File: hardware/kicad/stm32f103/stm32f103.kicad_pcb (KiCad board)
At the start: 2 copper layers, 67.3 x 69.2 mm, 114 parts, among them IC1 AT24CS02-SSHM, K1 RELAY_1RT, K2 RELAY_1RT, P1 5VIN, P10 SWD, P2 LOOP1, P3 LOOP2, P4 RELAY OUT 1, P5 TTL OUT 1, P6 RELAY OUT 2, P7 TTL OUT 2, P8 UART, P9 I2C, Q1 BSS138, Q2 BC817-40, Q3 BSS138, Q4 BC817-40, Q5 BC817-40, Q6 BC817-40, Q7 BC817-40, Q8 BC817-40, SW1 TACTILE_SW, SW2 TACTILE_SW, SW3 RESET, T1 78601/9C, T2 78601/9C, U1 LM1117-3.3, U2 STM32F030F4Px, U3 MCP23017, Y1 12MHz

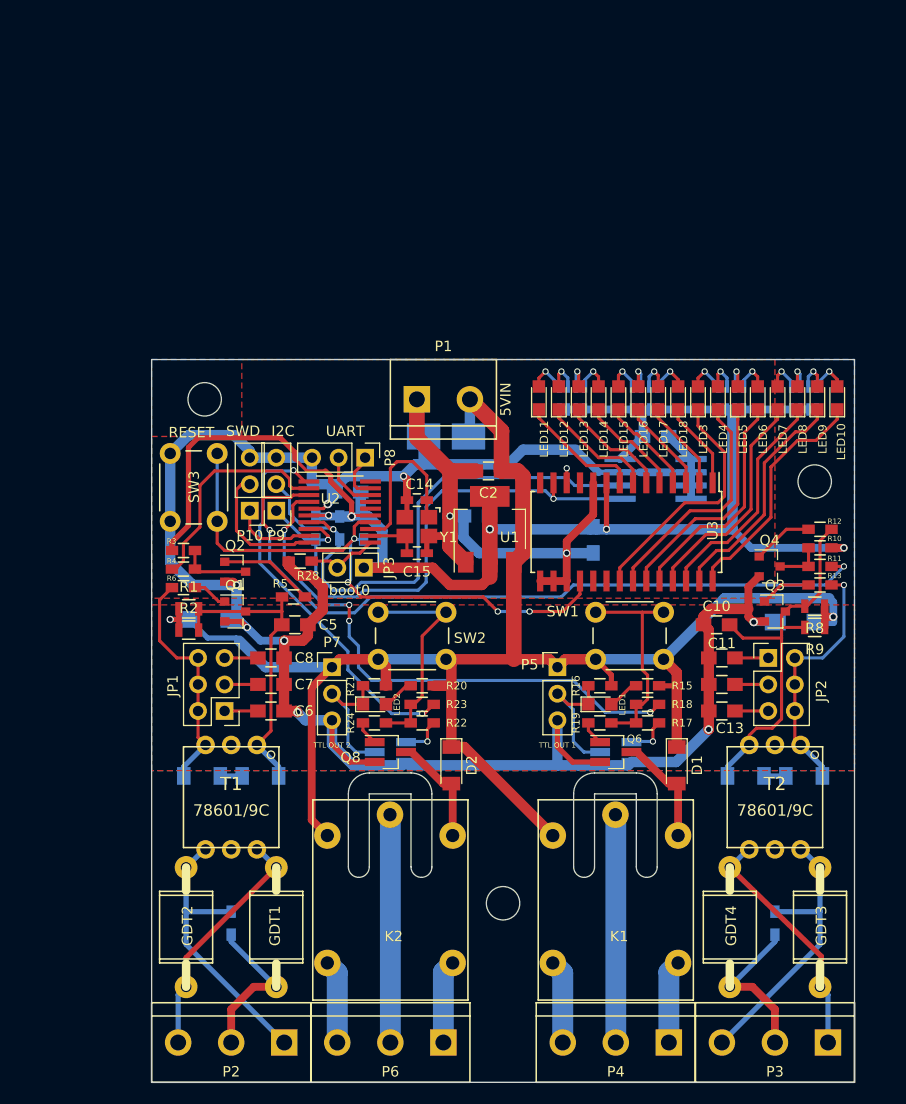
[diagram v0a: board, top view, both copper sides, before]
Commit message: hardware/kicad/stm32f103: MCU/LED block ready
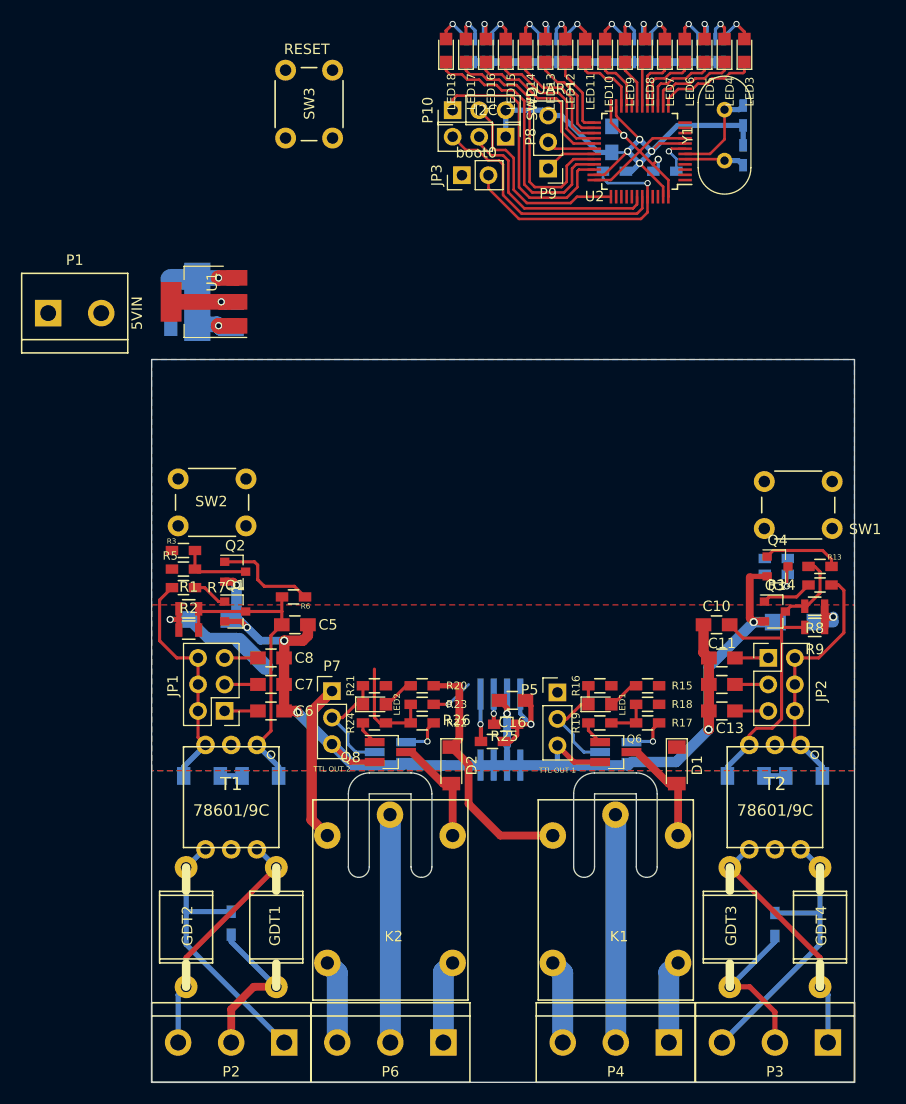
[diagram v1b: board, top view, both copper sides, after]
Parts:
- removed C18: 100n, Capacitors_SMD:C_0805_HandSoldering
- removed REF** (x3): MountingHole_3.2mm_M3, Mounting_Holes:MountingHole_3.2mm_M3
- removed U3: MCP23017, Housings_SOIC:SOIC-28W_7.5x17.9mm_Pitch1.27mm
- C14, C15, C2, R10, R12, R28: moved to B.Cu
- C16, R26: moved to F.Cu
- P8: value UART -> I2C
- P9: value I2C -> UART
- R11, R4: value 4.7k -> 1.8M; moved to B.Cu
- R13, R6: value 1k -> 4.7k
- R14, R7: value 1.8M -> 1k; moved to F.Cu
- R25: value 10k -> 4.7k; moved to F.Cu
- R27: value 4.7k -> 10k
- U2: value STM32F030F4Px -> STM32F103C8Tx; footprint Housings_SSOP:TSSOP-20_4.4x6.5mm_Pitch0.65mm_Handsoldering -> Housings_QFP:LQFP-48_7x7mm_Pitch0.5mm
- Y1: value 12MHz -> Crystal_Small; footprint Crystals:Crystal_SMD_3225_4Pads -> Crystals:Crystal_HC49-U_Vertical
- moved C15 52.3 mm to (92.2, 69.3), turned to 270 degrees
- moved R28 48.0 mm to (79.9, 74.7), turned to 0 degrees
- moved R27 47.8 mm to (84.7, 74.7), turned to 0 degrees
- moved Y1 45.8 mm to (90.4, 73.7), turned to 90 degrees
- moved C14 45.5 mm to (92.2, 73.2), turned to 90 degrees
- moved U2 44.9 mm to (82.3, 72.8)
- moved P10 43.0 mm to (64.4, 68.8), turned to 90 degrees
- moved P9 41.9 mm to (73.5, 74.4)
- moved LED18 40.0 mm to (63.8, 63.1)
- moved LED10 40.0 mm to (79.0, 63.1)
- moved JP3 38.7 mm to (65.3, 75.1), turned to 90 degrees
- moved C17 38.4 mm to (79.6, 71.6)
- moved SW3 38.3 mm to (48.4, 71.5)
- moved LED17 38.0 mm to (65.7, 63.1)
- moved LED9 38.0 mm to (80.9, 63.1)
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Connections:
- GDT4 pad 1: Net-(GDT3-Pad2) -> Net-(GDT4-Pad1)
- GDT4 pad 2: Net-(GDT4-Pad2) -> Net-(GDT3-Pad1)
- LED10 pad 1: Net-(LED10-Pad1) -> /MCU/LD18
- LED11 pad 1: Net-(LED11-Pad1) -> /MCU/LD21
- LED12 pad 1: Net-(LED12-Pad1) -> /MCU/LD22
- LED13 pad 1: Net-(LED13-Pad1) -> /MCU/LD23
- LED14 pad 1: Net-(LED14-Pad1) -> /MCU/LD24
- LED15 pad 1: Net-(LED15-Pad1) -> /MCU/LD25
- LED16 pad 1: Net-(LED16-Pad1) -> /MCU/LD26
- LED17 pad 1: Net-(LED17-Pad1) -> /MCU/LD27
- LED18 pad 1: Net-(LED18-Pad1) -> /MCU/LD28
- LED3 pad 1: Net-(LED3-Pad1) -> /MCU/LD11
- LED4 pad 1: Net-(LED4-Pad1) -> /MCU/LD12
- LED5 pad 1: Net-(LED5-Pad1) -> /MCU/LD13
- LED6 pad 1: Net-(LED6-Pad1) -> /MCU/LD14
- LED7 pad 1: Net-(LED7-Pad1) -> /MCU/LD15
- LED8 pad 1: Net-(LED8-Pad1) -> /MCU/LD16
- LED9 pad 1: Net-(LED9-Pad1) -> /MCU/LD17
- P3 pad 1: Net-(GDT3-Pad2) -> Net-(GDT3-Pad1)
- P3 pad 2: Net-(GDT4-Pad2) -> Net-(GDT3-Pad2)
- P3 pad 3: Net-(GDT3-Pad1) -> Net-(GDT4-Pad1)
- P8 pad 1: /MCU/RXD -> GND
- P8 pad 2: /MCU/TXD -> /EEPROM/scl
- P8 pad 3: GND -> /EEPROM/sda
- P9 pad 1: /EEPROM/sda -> /MCU/RXD
- P9 pad 2: /EEPROM/scl -> /MCU/TXD
- R11 pad 1: /colpitts/osc1 -> Net-(GDT4-Pad1)
- R11 pad 2: Net-(Q4-Pad3) -> Net-(GDT3-Pad2)
- R12 pad 1: Net-(C10-Pad1) -> /colpitts/osc1
- R12 pad 2: Net-(Q4-Pad1) -> Net-(Q4-Pad3)
- R13 pad 1: Net-(Q3-Pad1) -> Net-(C10-Pad1)
- R13 pad 2: Net-(JP2-Pad2) -> Net-(Q4-Pad1)
- R14 pad 1: Net-(GDT3-Pad1) -> Net-(Q3-Pad1)
- R14 pad 2: Net-(GDT4-Pad2) -> Net-(JP2-Pad2)
- R25 pad 2: /MCU/reset -> /EEPROM/scl
- R26 pad 2: /EEPROM/scl -> /EEPROM/sda
- R27 pad 2: /EEPROM/sda -> Net-(R27-Pad2)
- R4 pad 1: /MCU/osc1 -> Net-(GDT2-Pad1)
- R4 pad 2: Net-(Q2-Pad3) -> Net-(GDT1-Pad2)
- R5 pad 1: Net-(C5-Pad1) -> /MCU/osc1
- R5 pad 2: Net-(Q2-Pad1) -> Net-(Q2-Pad3)
- R6 pad 1: Net-(Q1-Pad1) -> Net-(C5-Pad1)
- R6 pad 2: Net-(JP1-Pad2) -> Net-(Q2-Pad1)
- R7 pad 1: Net-(GDT2-Pad1) -> Net-(Q1-Pad1)
- R7 pad 2: Net-(GDT1-Pad2) -> Net-(JP1-Pad2)
- RN1 pad 1: Net-(LED3-Pad2) -> Net-(LED6-Pad2)
- RN1 pad 2: Net-(LED4-Pad2) -> Net-(LED5-Pad2)
- RN1 pad 3: Net-(LED5-Pad2) -> Net-(LED4-Pad2)
- RN1 pad 4: Net-(LED6-Pad2) -> Net-(LED3-Pad2)
- RN2 pad 1: Net-(LED7-Pad2) -> Net-(LED10-Pad2)
- RN2 pad 2: Net-(LED8-Pad2) -> Net-(LED9-Pad2)
- RN2 pad 3: Net-(LED9-Pad2) -> Net-(LED8-Pad2)
- RN2 pad 4: Net-(LED10-Pad2) -> Net-(LED7-Pad2)
- RN3 pad 1: Net-(LED11-Pad2) -> Net-(LED14-Pad2)
- RN3 pad 2: Net-(LED12-Pad2) -> Net-(LED13-Pad2)
- RN3 pad 3: Net-(LED13-Pad2) -> Net-(LED12-Pad2)
- RN3 pad 4: Net-(LED14-Pad2) -> Net-(LED11-Pad2)
- RN4 pad 1: Net-(LED15-Pad2) -> Net-(LED18-Pad2)
- RN4 pad 2: Net-(LED16-Pad2) -> Net-(LED17-Pad2)
- RN4 pad 3: Net-(LED17-Pad2) -> Net-(LED16-Pad2)
- RN4 pad 4: Net-(LED18-Pad2) -> Net-(LED15-Pad2)
- SW3 pad 2: /MCU/reset -> Net-(R27-Pad2)
- T2 pad 4: Net-(GDT3-Pad2) -> Net-(GDT3-Pad1)
- T2 pad 6: Net-(GDT3-Pad1) -> Net-(GDT4-Pad1)
- U2 pad 1: Net-(JP3-Pad2) -> (no net)
- U2 pad 10: (no net) -> /MCU/osc1
- U2 pad 11: /MCU/active1 -> (no net)
- U2 pad 12: /MCU/osc1 -> /colpitts/osc1
- U2 pad 13: /colpitts/osc1 -> /MCU/LD11
- U2 pad 14: /outputs/active1 -> /MCU/LD12
- U2 pad 15: GND -> /MCU/LD13
- U2 pad 16: +3V3 -> /MCU/LD14
- U2 pad 17: /EEPROM/scl -> /MCU/LD15
- U2 pad 18: /EEPROM/sda -> /MCU/LD16
- U2 pad 19: /MCU/SWD -> /MCU/LD17
- U2 pad 2: Net-(C15-Pad1) -> (no net)
- U2 pad 20: /MCU/SWC -> (no net)
- U2 pad 3: Net-(C14-Pad1) -> /MCU/active1
- U2 pad 4: /MCU/reset -> /outputs/active1
- U2 pad 5: +3V3 -> Net-(C14-Pad1)
- U2 pad 6: (no net) -> Net-(C15-Pad1)
- U2 pad 7: (no net) -> Net-(R27-Pad2)
- U2 pad 8: /MCU/TXD -> GND
- U2 pad 9: /MCU/RXD -> +3V3
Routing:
- net +5V: track 169.3 -> 67.3 mm, vias 2 -> 3
- net GND: track 272.5 -> 177.1 mm, vias 10 -> 12
- net +3V3: track 155.9 -> 67.1 mm, vias 5 -> 4
- net /colpitts/osc1: track 70.8 -> 0.00 mm, vias 2 -> 0
- net /MCU/reset: track 56.1 -> 0.00 mm, vias 4 -> 0
- net /outputs/active1: track 52.8 -> 0.00 mm, vias 4 -> 0
- net /MCU/active1: track 37.6 -> 4.13 mm, vias 2 -> 1
- net /EEPROM/scl: track 56.8 -> 23.9 mm, vias 2 -> 1
- net Net-(GDT4-Pad1): track 0.00 -> 27.6 mm
- net /MCU/LD28: track 0.00 -> 26.5 mm
- net /EEPROM/sda: track 53.4 -> 28.8 mm, vias 2 -> 1
- net /MCU/LD27: track 0.00 -> 24.4 mm
- net Net-(LED3-Pad1): track 23.5 -> 0.00 mm
- net Net-(LED10-Pad1): track 22.9 -> 0.00 mm
- net Net-(LED4-Pad1): track 22.6 -> 0.00 mm
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- removed copper zone on F.Cu, net +3V3
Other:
- net class Default: clearance 0.25 -> 0.17; trace_width 0.3 -> 0.25
- net class Power: clearance 0.25 -> 0.24
- rule trace_clearance: 0.25 -> 0.17

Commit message: hardware/kicad/stm32f103: Almost there...
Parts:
- added REF**: MountingHole_3.2mm_M3, Mounting_Holes:MountingHole_3.2mm_M3, F.Cu at (98.8, 101.6)
- added REF**: MountingHole_3.2mm_M3, Mounting_Holes:MountingHole_3.2mm_M3, F.Cu at (39.6, 101.6)
- added REF**: MountingHole_3.2mm_M3, Mounting_Holes:MountingHole_3.2mm_M3, F.Cu at (69.2, 144.7)
- C16: moved to B.Cu
- C17: moved to F.Cu
- moved SW3 55.7 mm to (89.4, 109.2)
- moved C17 48.9 mm to (70.1, 119.6), turned to 180 degrees
- moved R28 40.9 mm to (64.3, 112.5), turned to 90 degrees
- moved JP3 38.0 mm to (59.7, 112.6)
- moved LED17 38.0 mm to (60.1, 100.7)
- moved LED4 38.0 mm to (84.8, 100.7)
- moved LED5 38.0 mm to (82.9, 100.7)
- moved LED6 38.0 mm to (81.0, 100.7)
- moved LED7 38.0 mm to (79.1, 100.7)
- moved LED8 38.0 mm to (77.2, 100.7)
- moved P9 38.0 mm to (67.9, 112.0)
- moved R27 38.0 mm to (79.1, 112.3)
- moved RN3 38.0 mm to (68.3, 100.7)
- moved U2 38.0 mm to (76.7, 110.4)
- moved Y1 38.0 mm to (84.8, 111.3)
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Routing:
- net +5V: track 67.3 -> 183.3 mm
- net +3V3: track 67.1 -> 145.9 mm, vias 4 -> 5
- net /MCU/osc1: track 0.00 -> 55.1 mm, vias 0 -> 2
- net GND: track 177.1 -> 224.1 mm
- net /MCU/active1: track 4.13 -> 33.9 mm, vias 1 -> 2
- net Net-(R27-Pad2): track 3.86 -> 27.3 mm
- net /outputs/active1: track 0.00 -> 18.7 mm, vias 0 -> 2
- net /colpitts/osc1: track 0.00 -> 17.7 mm, vias 0 -> 1
- net Net-(R17-Pad2): track 4.15 -> 15.6 mm
- net Net-(R22-Pad2): track 10.1 -> 16.5 mm
- net Net-(JP3-Pad2): track 25.9 -> 22.3 mm, vias 1 -> 0
- net /EEPROM/scl: track 23.9 -> 27.5 mm, vias 1 -> 2
- net /EEPROM/sda: track 28.8 -> 31.8 mm, vias 1 -> 2
- net Net-(LED2-Pad1): track 11.3 -> 9.71 mm
- added copper zone on F.Cu, net +3V3
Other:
- board size 67.3 x 69.2 mm -> 67.3 x 64.4 mm

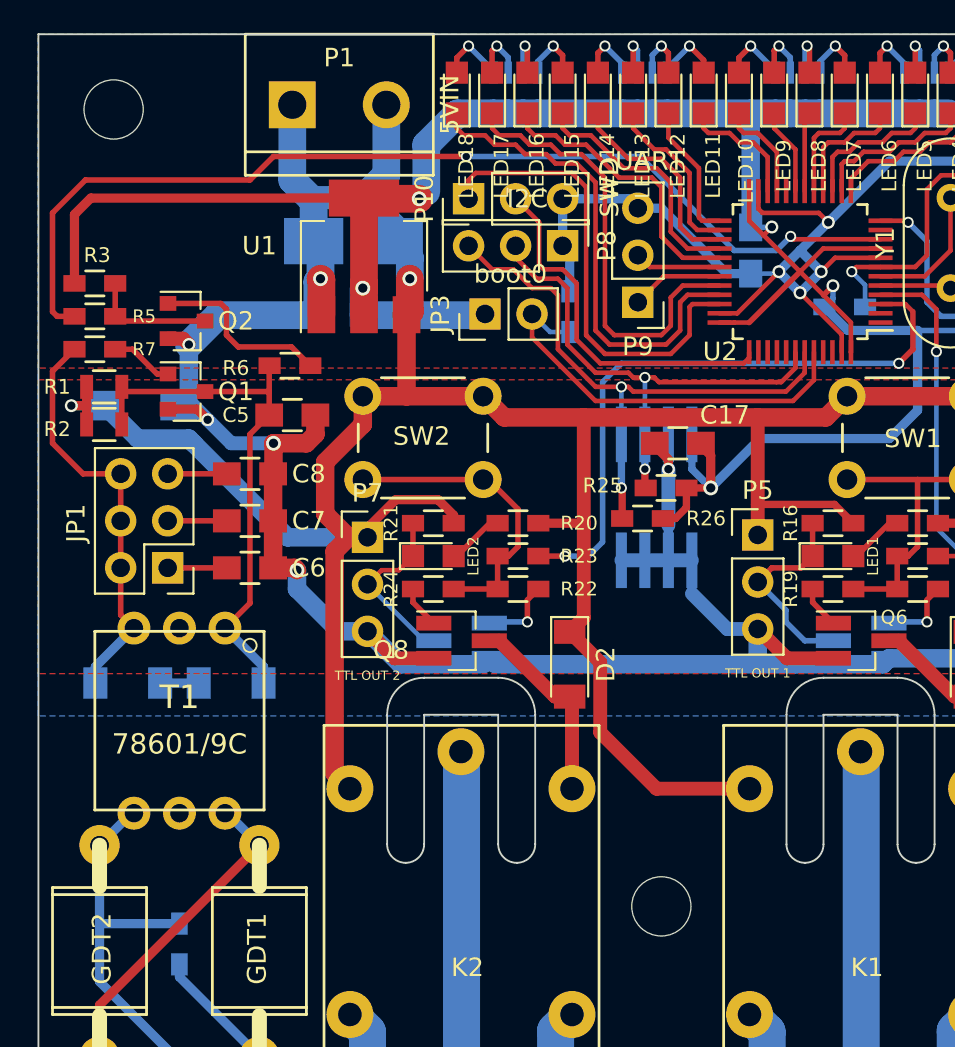
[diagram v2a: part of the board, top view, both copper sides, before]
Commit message: hardware/kicad/stm32f103: Minor cosmetic changes
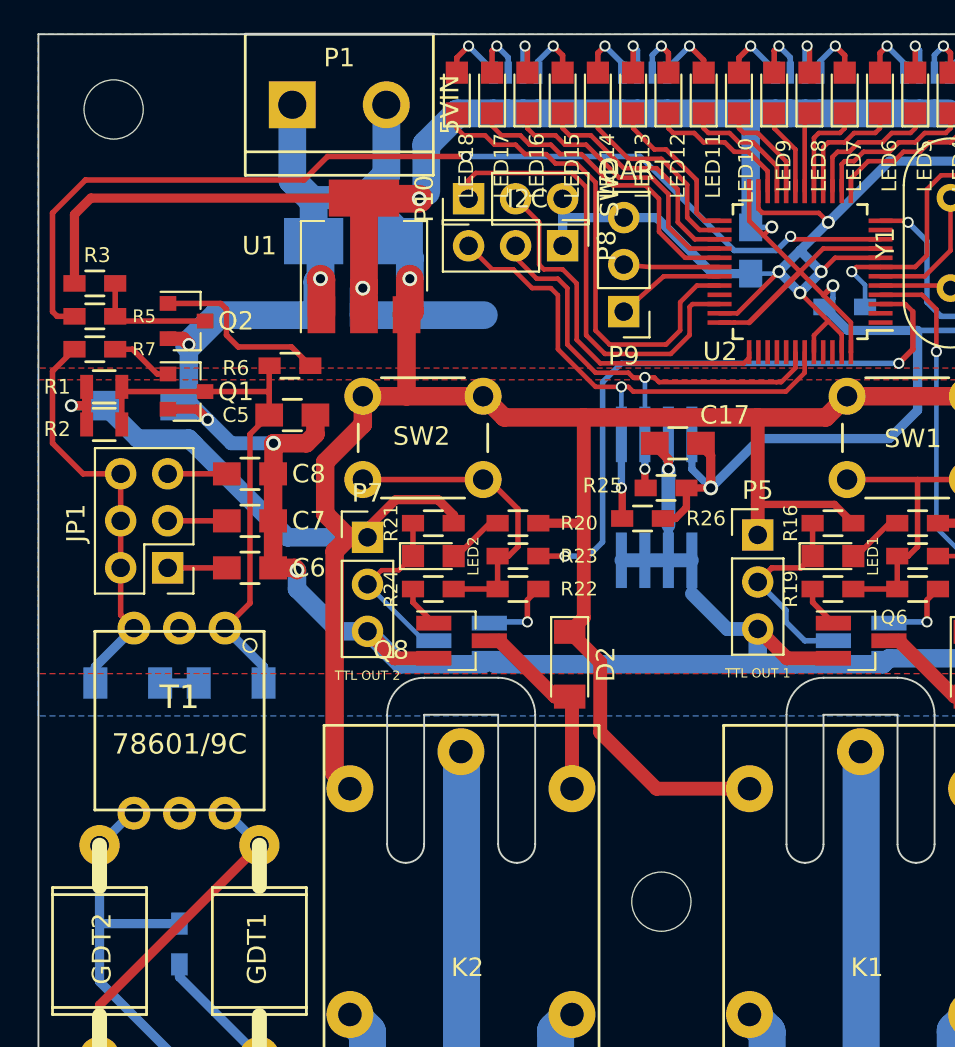
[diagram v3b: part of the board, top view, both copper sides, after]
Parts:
- removed JP3: boot0, Pin_Headers:Pin_Header_Straight_1x02_Pitch2.54mm
- removed R28: 10k, Resistors_SMD:R_0603_HandSoldering
- Y1: value Crystal_Small -> 8MHz
- moved P9 0.92 mm to (67.2, 112.5)
- moved REF** 0.25 mm to (69.2, 144.4)
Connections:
- U2 pad 20: (no net) -> /MCU/LD18
- U2 pad 21: /MCU/LD18 -> /MCU/LD21
- U2 pad 22: /MCU/LD21 -> /MCU/LD22
- U2 pad 25: /MCU/LD22 -> /MCU/LD23
- U2 pad 26: /MCU/LD23 -> /MCU/LD24
- U2 pad 27: /MCU/LD24 -> /MCU/LD25
- U2 pad 28: /MCU/LD25 -> /MCU/LD26
- U2 pad 29: /MCU/LD26 -> /MCU/LD27
- U2 pad 32: /MCU/LD27 -> /MCU/LD28
- U2 pad 33: /MCU/LD28 -> (no net)
- U2 pad 44: Net-(JP3-Pad2) -> GND
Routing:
- net Net-(JP3-Pad2): track 22.3 -> 0.00 mm
- net /MCU/LD27: track 24.4 -> 17.0 mm
- net GND: track 224.1 -> 223.1 mm
- net /MCU/RXD: track 4.99 -> 5.90 mm
- net /MCU/LD24: track 11.4 -> 10.7 mm
- net /MCU/LD25: track 13.5 -> 12.8 mm
- net /MCU/LD26: track 15.6 -> 14.9 mm
- net /MCU/LD23: track 9.31 -> 8.58 mm
- net /MCU/LD22: track 7.50 -> 8.21 mm
- net /MCU/TXD: track 4.68 -> 5.18 mm
